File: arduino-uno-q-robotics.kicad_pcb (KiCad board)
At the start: 4 copper layers, 68.6 x 53.3 mm, 15 parts, among them J1 Conn_02x30_Odd_Even, J2 Conn_02x30_Odd_Even, J3 Connector_FFC-FPC, J5 Conn_02x30_Odd_Even, U1 LSM6DSO32, U2 TCA9803

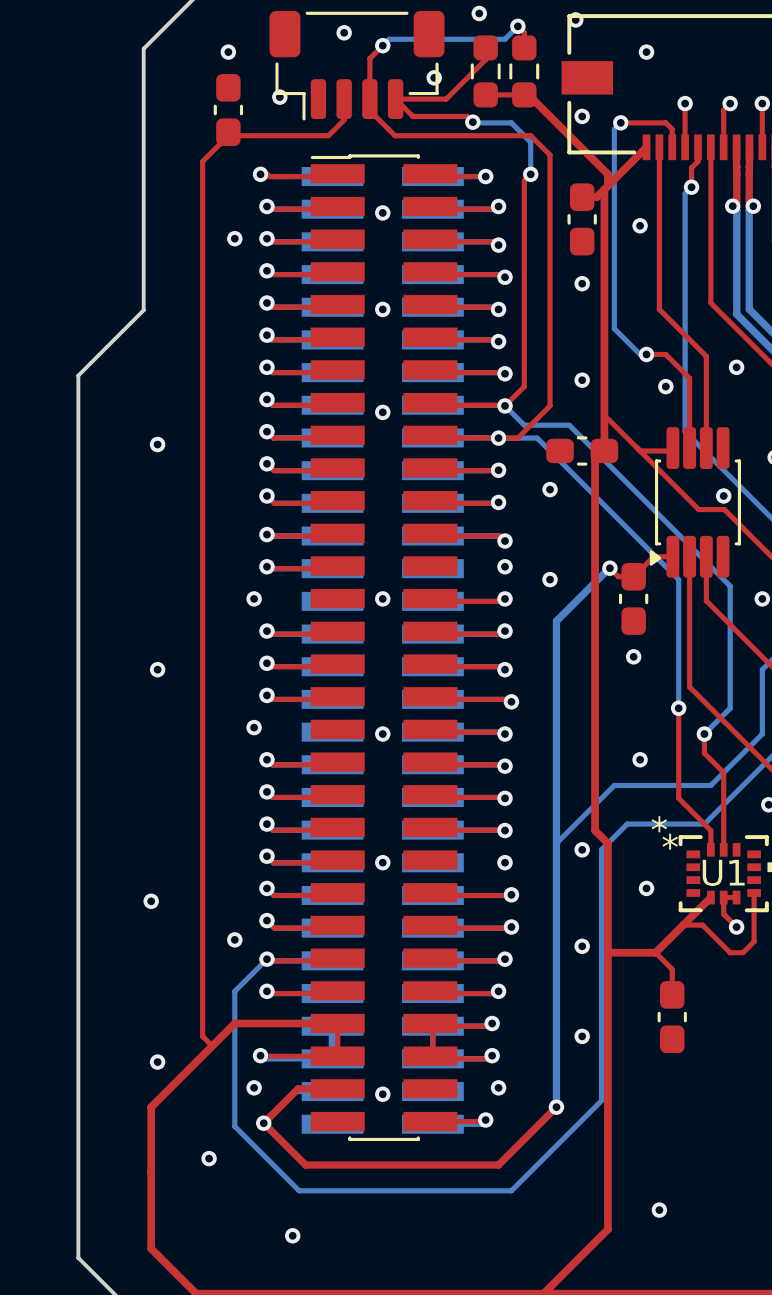
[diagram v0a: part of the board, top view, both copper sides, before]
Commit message: Adjust JMISC header position
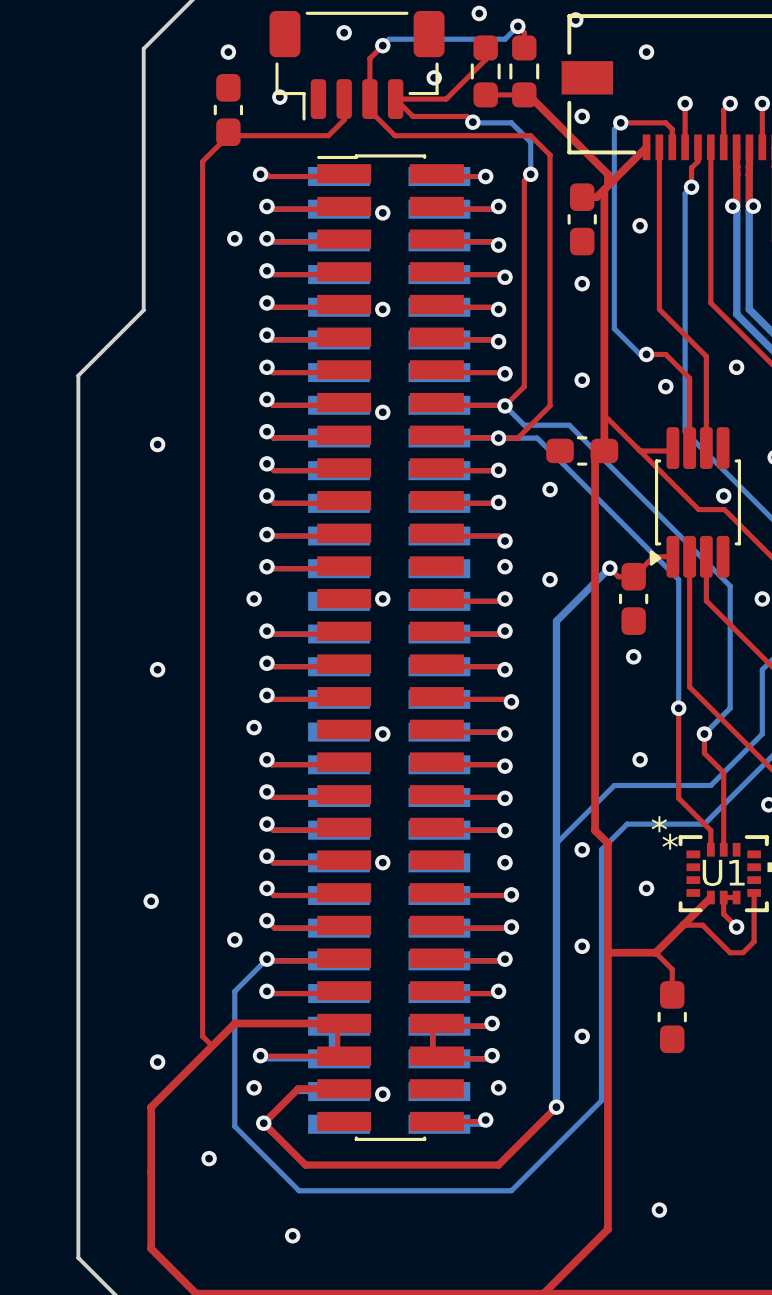
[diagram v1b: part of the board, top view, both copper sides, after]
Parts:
- moved J5 0.25 mm to (128.1, 93.4)
- moved J1 0.25 mm to (126.5, 93.5)
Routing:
- net /MCU_PSSI_D0: track 6.95 -> 5.90 mm
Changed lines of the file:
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@@
 	(footprint "Connector_PinSocket_1.27mm:PinSocket_2x30_P1.27mm_Vertical_SMD"
 		(layer "F.Cu")
-		(at 127.8 93.395)
+		(at 128.05 93.395)
 		(descr "surface-mounted straight socket strip, 2x30, 1.27mm pitch, double cols (from Kicad 4.0.7!), script generated")
 		(tags "Surface mounted socket strip SMD 2x30 1.27mm double row")
@@
 	(footprint "Connector_PinHeader_1.27mm:PinHeader_2x30_P1.27mm_Vertical_SMD"
 		(layer "B.Cu")
-		(at 126.25 93.5 180)
+		(at 126.5 93.5 180)
 		(descr "surface-mounted straight pin header, 2x30, 1.27mm pitch, double rows")
 		(tags "Surface mounted pin header SMD 2x30 1.27mm double row")
@@
 		(width 0.2)
 		(layer "B.Cu")
-		(net 24)
-	)
-	(segment
-		(start 123.25 75)
-		(end 124.3 75)
-		(width 0.2)
-		(layer "B.Cu")

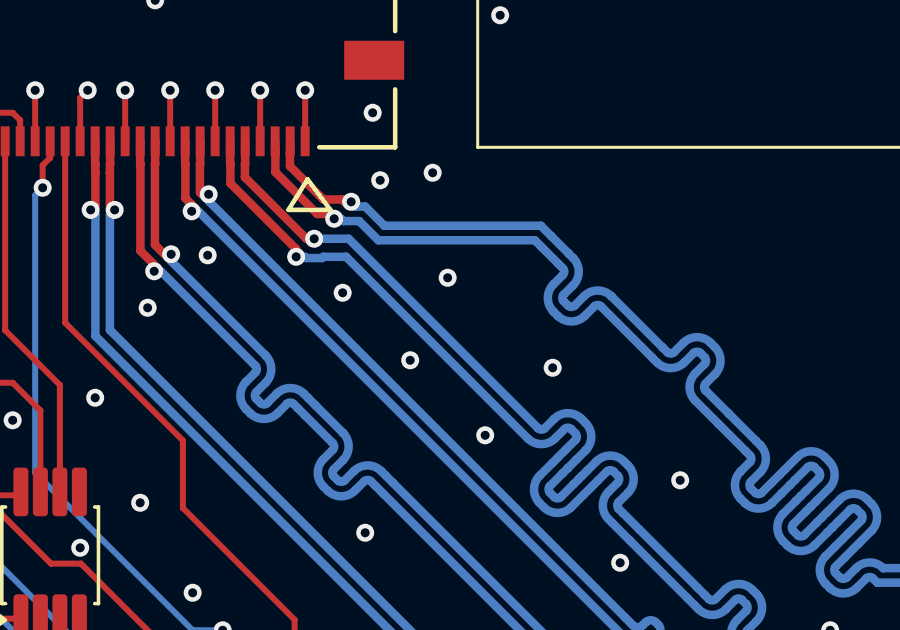
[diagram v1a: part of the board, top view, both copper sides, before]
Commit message: Adjust differential camera pairs length
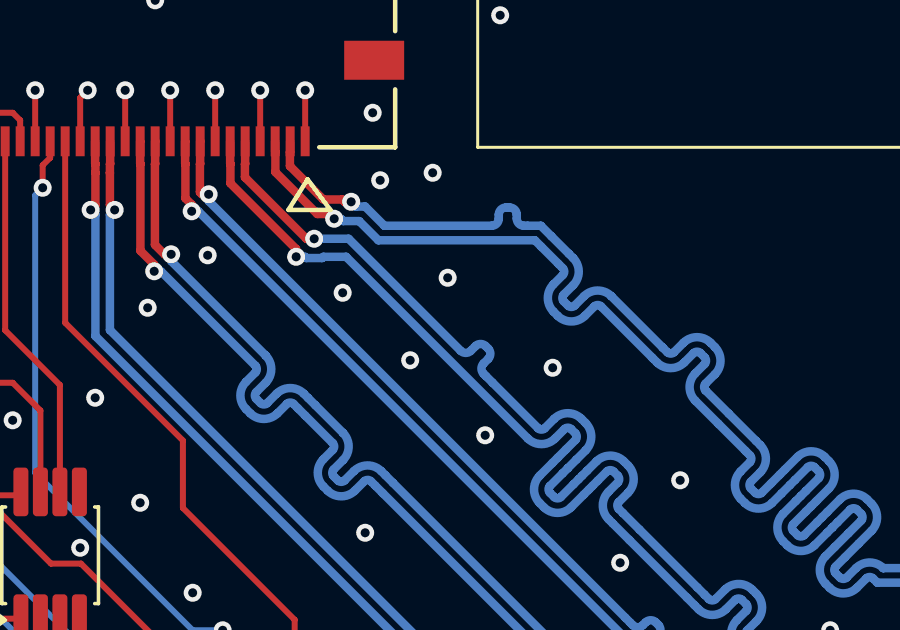
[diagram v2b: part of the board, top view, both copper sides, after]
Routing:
- net /CSI0_LN1_N: track 44.3 -> 45.3 mm
- net /CSI0_LN0_N: track 45.2 -> 46.0 mm
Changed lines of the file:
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@@
 	)
 	(segment
+		(start 153.453582 76.5258)
+		(end 153.453582 76.398522)
+		(width 0.2832)
+		(layer "B.Cu")
+		(net 78)
+	)
+	(segment
 		(start 159.607982 80.667781)
 		(end 159.29537 80.980392)
@@
 	)
 	(segment
-		(start 148.691243 76.125557)
-		(end 148.532843 75.967157)
-		(width 0.2832)
-		(layer "B.Cu")
-		(net 78)
-	)
-	(segment
 		(start 155.760381 79.425302)
 		(end 155.618959 79.28388)
@@
 	)
 	(segment
+		(start 154.413582 76.7658)
+		(end 154.857474 76.7658)
+		(width 0.2832)
+		(layer "B.Cu")
+		(net 78)
+	)
+	(segment
 		(start 155.618959 79.060574)
 		(end 155.931569 78.747961)
@@
 	)
 	(segment
+		(start 148.691243 76.125557)
+		(end 148.999579 76.125557)
+		(width 0.2832)
+		(layer "B.Cu")
+		(net 78)
+	)
+	(segment
 		(start 164.059443 86.652532)
 		(end 163.635179 87.076796)
@@
 	)
 	(segment
+		(start 154.293582 76.7658)
+		(end 154.413582 76.7658)
+		(width 0.2832)
+		(layer "B.Cu")
+		(net 78)
+	)
+	(segment
 		(start 163.270453 86.71207)
 		(end 163.694716 86.287804)
@@
 	)
 	(segment
+		(start 149.639822 76.7658)
+		(end 153.213582 76.7658)
+		(width 0.2832)
+		(layer "B.Cu")
+		(net 78)
+	)
+	(segment
 		(start 157.204364 79.11269)
 		(end 157.204362 79.11269)
@@
 	)
 	(segment
+		(start 153.693582 76.158522)
+		(end 153.813582 76.158522)
+		(width 0.2832)
+		(layer "B.Cu")
+		(net 78)
+	)
+	(segment
 		(start 163.411875 87.076796)
 		(end 163.270453 86.935374)
@@
 	(segment
 		(start 148.999579 76.125557)
-		(end 148.691243 76.125557)
+		(end 149.639822 76.7658)
 		(width 0.2832)
 		(layer "B.Cu")
@@
 	)
 	(segment
-		(start 149.639822 76.7658)
-		(end 148.999579 76.125557)
+		(start 154.053582 76.398522)
+		(end 154.053582 76.5258)
+		(width 0.2832)
+		(layer "B.Cu")
+		(net 78)
+	)
+	(segment
+		(start 154.857474 76.7658)
+		(end 155.205867 77.114193)
 		(width 0.2832)
 		(layer "B.Cu")
@@
 	)
 	(segment
-		(start 154.857474 76.7658)
-		(end 149.639822 76.7658)
-		(width 0.2832)
-		(layer "B.Cu")
-		(net 78)
-	)
-	(segment
 		(start 158.930645 80.838972)
 		(end 158.903086 80.811412)
@@
 	)
 	(segment
-		(start 155.205867 77.114193)
-		(end 154.857474 76.7658)
-		(width 0.2832)
-		(layer "B.Cu")
-		(net 78)
-	)
-	(segment
 		(start 165.362007 88.178399)
 		(end 165.049396 88.491011)
@@
 		(net 78)
 	)
+	(segment
+		(start 148.532843 75.967157)
+		(end 148.691243 76.125557)
+		(width 0.2832)
+		(layer "B.Cu")
+		(net 78)
+	)
+	(arc
+		(start 154.053582 76.5258)
+		(mid 154.123876 76.695506)
+		(end 154.293582 76.7658)
+		(width 0.2832)
+		(layer "B.Cu")
+		(net 78)
+	)
 	(arc
 		(start 155.931569 78.747961)
@@
 	)
 	(arc
+		(start 153.453582 76.398522)
+		(mid 153.523876 76.228816)
+		(end 153.693582 76.158522)
+		(width 0.2832)
+		(layer "B.Cu")
+		(net 78)
+	)
+	(arc
+		(start 153.813582 76.158522)
+		(mid 153.983288 76.228816)
+		(end 154.053582 76.398522)
+		(width 0.2832)
+		(layer "B.Cu")
+		(net 78)
+	)
+	(arc
+		(start 153.213582 76.7658)
+		(mid 153.383288 76.695506)
+		(end 153.453582 76.5258)
+		(width 0.2832)
+		(layer "B.Cu")
+		(net 78)
+	)
+	(arc
 		(start 160.657469 81.717268)
 		(mid 160.845536 81.263235)
@@
 	)
 	(segment
+		(start 153.016843 80.777536)
+		(end 153.101695 80.862388)
+		(width 0.2832)
+		(layer "B.Cu")
+		(net 89)
+	)
+	(segment
 		(start 157.45109 86.201091)
 		(end 157.592513 86.342515)
@@
 	)
 	(segment
+		(start 152.946452 81.696453)
+		(end 153.031306 81.781306)
+		(width 0.2832)
+		(layer "B.Cu")
+		(net 89)
+	)
+	(segment
 		(start 160.9934 88.894873)
 		(end 160.680788 89.207484)
@@
 	)
 	(segment
+		(start 153.101695 81.2018)
+		(end 152.946451 81.357041)
+		(width 0.2832)
+		(layer "B.Cu")
+		(net 89)
+	)
+	(segment
 		(start 157.763702 85.665175)
 		(end 157.451091 85.977787)
@@
 	)
 	(segment
+		(start 148.449479 77.199479)
+		(end 152.182778 80.932778)
+		(width 0.2832)
+		(layer "B.Cu")
+		(net 89)
+	)
+	(segment
 		(start 160.074379 88.824379)
 		(end 158.147258 86.897258)
@@
 	)
 	(segment
-		(start 148.449479 77.199479)
-		(end 154.764087 83.514087)
-		(width 0.2832)
-		(layer "B.Cu")
-		(net 89)
-	)
-	(segment
 		(start 161.730277 90.480277)
 		(end 161.730276 90.480278)
@@
 	)
 	(segment
+		(start 153.248643 81.998643)
+		(end 154.764087 83.514087)
+		(width 0.2832)
+		(layer "B.Cu")
+		(net 89)
+	)
+	(segment
+		(start 147.300521 77.199479)
+		(end 148.449479 77.199479)
+		(width 0.2832)
+		(layer "B.Cu")
+		(net 89)
+	)
+	(segment
 		(start 155.158581 85.665176)
 		(end 155.300002 85.806597)
@@
 	)
 	(segment
-		(start 147.300521 77.199479)
-		(end 148.449479 77.199479)
-		(width 0.2832)
-		(layer "B.Cu")
-		(net 89)
-	)
-	(segment
 		(start 169.356599 91.9884)
 		(end 167.513147 91.9884)
@@
 	)
 	(segment
+		(start 153.031306 81.781306)
+		(end 153.248643 81.998643)
+		(width 0.2832)
+		(layer "B.Cu")
+		(net 89)
+	)
+	(segment
 		(start 156.208069 83.201477)
 		(end 156.34949 83.342898)
@@
 		(net 89)
 	)
+	(segment
+		(start 152.52219 80.932779)
+		(end 152.677431 80.777535)
+		(width 0.2832)
+		(layer "B.Cu")
+		(net 89)
+	)
 	(arc
 		(start 155.300003 83.201476)
@@
 	)
 	(arc
+		(start 153.101695 80.862388)
+		(mid 153.171989 81.032093)
+		(end 153.101695 81.2018)
+		(width 0.2832)
+		(layer "B.Cu")
+		(net 89)
+	)
+	(arc
+		(start 152.946451 81.357041)
+		(mid 152.876158 81.526747)
+		(end 152.946452 81.696453)
+		(width 0.2832)
+		(layer "B.Cu")
+		(net 89)
+	)
+	(arc
 		(start 165.871047 91.8305)
 		(mid 165.824799 91.942152)
@@
 	)
 	(arc
+		(start 152.182778 80.932778)
+		(mid 152.352484 81.003072)
+		(end 152.52219 80.932779)
+		(width 0.2832)
+		(layer "B.Cu")
+		(net 89)
+	)
+	(arc
 		(start 157.451091 85.977787)
 		(mid 157.404843 86.089439)
@@
 	)
 	(arc
+		(start 152.677431 80.777535)
+		(mid 152.847137 80.707242)
+		(end 153.016843 80.777536)
+		(width 0.2832)
+		(layer "B.Cu")
+		(net 89)
+	)
+	(arc
 		(start 155.300002 85.806597)
 		(mid 155.411655 85.852845)
@@
 		(base_line
 			(pts
+				(xy 152.182778 80.932778) (xy 153.248643 81.998643)
+			)
+		)
+		(base_line_coupled
+			(pts
+				(xy 151.840397 81.275159) (xy 151.827708 81.26247)
+			)
+		)
+		(corner_radius_percent 80)
+		(end
+			(xy 153.248643 81.998643)
+		)
+		(initial_side "left")
+		(last_diff_pair_gap 0.18)
+		(last_netname "/CSI0_LN1_N")
+		(last_status "tuned")
+		(last_track_width 0.2832)
+		(last_tuning "0.0000 mm (tuned)")
+		(max_amplitude 1)
+		(min_amplitude 0.2)
+		(min_spacing 0.6)
+		(origin
+			(xy 152.182778 80.932778)
+		)
+		(override_custom_rules no)
+		(rounded yes)
+		(single_sided no)
+		(target_length 1000000)
+		(target_length_max 1000000)
+		(target_length_min 0)
+		(target_skew 0)
+		(target_skew_max 0.1)
+		(target_skew_min -0.1)
+		(tuning_mode "diff_pair_skew")
+		(members "06d5b86d-6fc2-4df6-983a-b900a95fd668" "1187d318-e3a4-4dee-a6b8-6313afc2e587"
+			"124484e7-fb7c-4b2c-91ab-7cc476e8827d" "15620ee6-5a31-4861-b6bc-322023da78ba"
+			"2bc43379-d091-4da0-adf5-95caa6208f9e" "48ae3441-ff0a-44df-8cde-50820d07163e"
+			"7b96128e-0c50-4212-9d7f-58e1af472afd" "b75b43a0-3768-4d84-b9bf-74a2e0362f5a"
+			"f4018332-6245-48ff-b595-08d0186fe27a"
+		)
+	)
+	(generated
+		(type tuning_pattern)
+		(name "Tuning Pattern")
+		(layer "B.Cu")
+		(base_line
+			(pts
 				(xy 161.730277 90.480277) (xy 160.074379 88.824379)
 			)
@@
 		)
 	)
+	(generated
+		(type tuning_pattern)
+		(name "Tuning Pattern")
+		(layer "B.Cu")
+		(base_line
+			(pts
+				(xy 153.213582 76.7658) (xy 154.857474 76.7658)
+			)
+		)
+		(base_line_coupled
+			(pts
+				(xy 153.213582 77.25) (xy 153.188204 77.25)
+			)
+		)
+		(corner_radius_percent 80)
+		(end
+			(xy 154.857474 76.7658)
+		)
+		(initial_side "left")
+		(last_diff_pair_gap 0.18)
+		(last_netname "/CSI0_LN0_N")
+		(last_status "tuned")
+		(last_track_width 0.2832)
+		(last_tuning "0.0000 mm (tuned)")
+		(max_amplitude 1)
+		(min_amplitude 0.2)
+		(min_spacing 0.6)
+		(origin
+			(xy 153.213582 76.7658)
+		)
+		(override_custom_rules no)
+		(rounded yes)
+		(single_sided no)
+		(target_length 1000000)
+		(target_length_max 1000000)
+		(target_length_min 0)
+		(target_skew 0)
+		(target_skew_max 0.1)
+		(target_skew_min -0.1)
+		(tuning_mode "diff_pair_skew")
+		(members "00876e1d-62dd-4682-bc87-7573a490f4e1" "0d3c85e5-1a54-4535-a469-5a15660dcf36"
+			"4f639cc1-2ca3-4e33-ab0d-4f3c1ee2cf4e" "6a6a8623-08f8-49c5-9747-0360dc3bd987"
+			"6d8c6005-01eb-4737-ae78-bd416d6aa5d6" "726354f3-778d-48ca-8cf4-6dc4892e81ea"
+			"7ee5c3bb-f888-4db0-aa47-809125f0284d" "b2c40f14-19ff-4ff0-8450-13efeefe172a"
+			"c0636fa8-5e21-472d-a2b1-24058862e42d"
+		)
+	)
